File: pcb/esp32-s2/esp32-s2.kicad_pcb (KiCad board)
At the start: 2 copper layers, 31 parts, among them J1 BATT, J2 HALL-CONN, Q1 BC817, Q2 BC807, SW1 WIFI-Config, SW2 RST, U1 XC6220, U2 ESP32-S2-WROOM

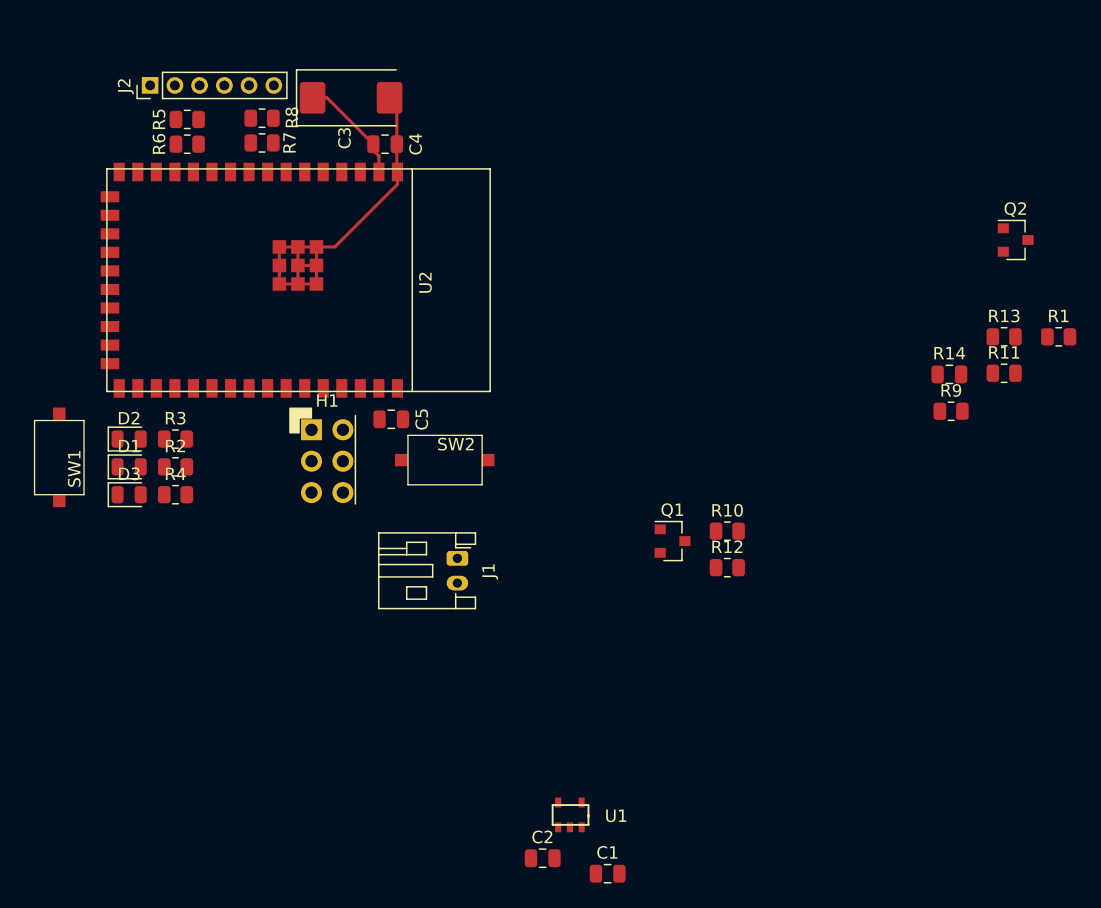
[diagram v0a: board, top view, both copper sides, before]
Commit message: update pcb for esp32s2
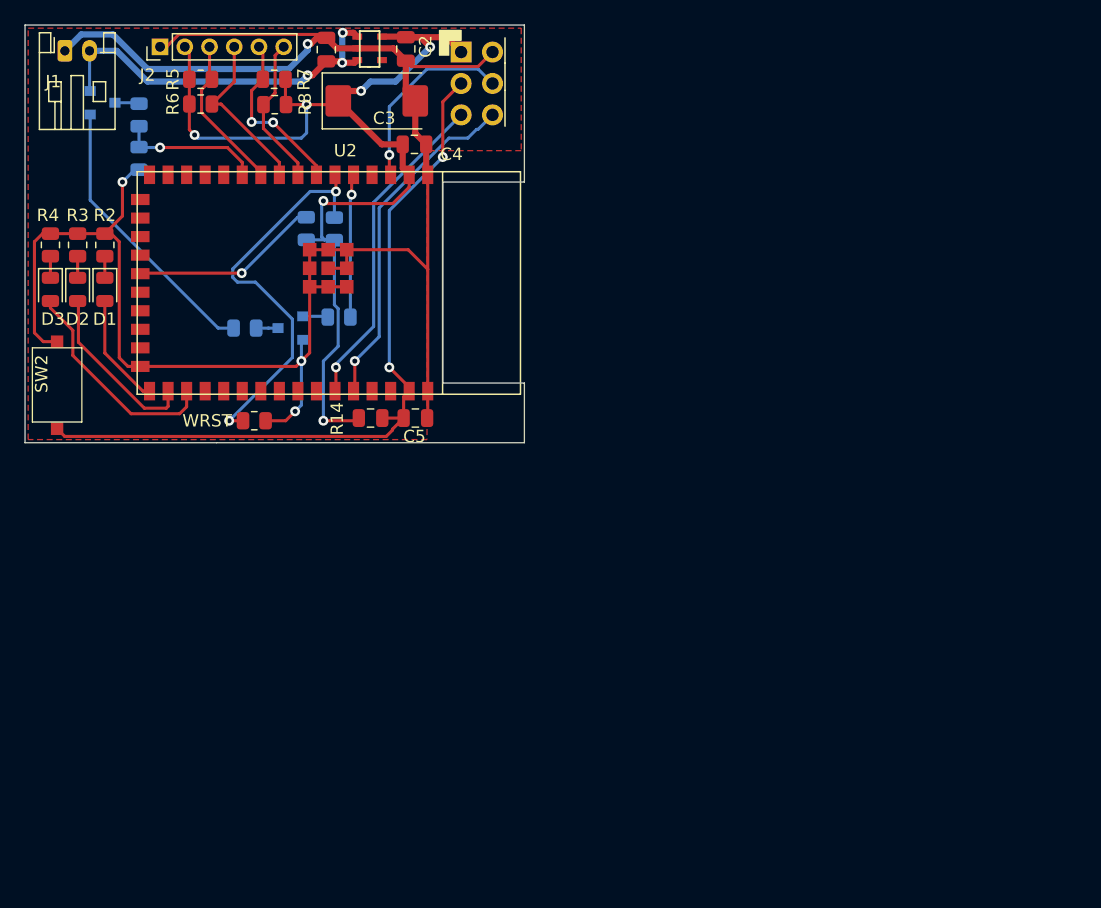
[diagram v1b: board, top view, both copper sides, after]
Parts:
- removed SW1: WIFI-Config, SMDButton:SMD_Button
- added R15: 0, Resistor_SMD:R_0805_2012Metric, F.Cu at (106.2, 86.9)
- Q1, Q2, R1, R10, R11, R12, R13, R9: moved to B.Cu
- moved Q2 74.7 mm to (93.9, 61.1)
- moved R13 71.4 mm to (96.8, 65.7), turned to 270 degrees
- moved C1 70.4 mm to (112.0, 56.9), turned to 90 degrees
- moved C2 66.4 mm to (118.4, 56.8), turned to 270 degrees
- moved U1 64.0 mm to (115.5, 56.8), turned to 270 degrees
- moved R11 61.5 mm to (105.4, 79.4)
- moved R1 61.5 mm to (110.4, 71.3), turned to 90 degrees
- moved R12 60.0 mm to (96.8, 62.1), turned to 270 degrees
- moved R9 52.0 mm to (112.7, 71.3), turned to 270 degrees
- moved J1 51.9 mm to (90.8, 57.0), turned to 0 degrees
- moved R14 46.9 mm to (115.6, 86.7)
- moved R10 35.9 mm to (113.0, 78.5)
- moved Q1 35.4 mm to (109.1, 79.4), turned to 180 degrees
- moved H1 32.9 mm to (122.9, 57.0)
- moved SW2 32.0 mm to (90.4, 83.8), turned to 90 degrees
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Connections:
- U2 pad 10: HALL4 -> HALL3
- U2 pad 8: HALL2 -> HALL4
- U2 pad 9: HALL3 -> HALL2
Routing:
- net GND: track 32.4 -> 165.5 mm, vias 0 -> 4
- net VCC: track 8.90 -> 85.6 mm, vias 0 -> 6
- net /EN: track 0.00 -> 61.0 mm, vias 0 -> 2
- net Net-(R15-Pad2): track 0.00 -> 32.9 mm, vias 0 -> 2
- net BATT: track 0.00 -> 30.5 mm, vias 0 -> 3
- net /RX: track 0.00 -> 28.0 mm, vias 0 -> 1
- net /TX: track 0.00 -> 26.6 mm, vias 0 -> 1
- net Net-(Q2-Pad1): track 0.00 -> 22.8 mm
- net /Green: track 0.00 -> 17.8 mm
- net IO0: track 0.00 -> 15.6 mm, vias 0 -> 1
- net Net-(R1-Pad2): track 0.00 -> 15.3 mm, vias 0 -> 1
- net /Red: track 0.00 -> 14.1 mm
- net HALL1: track 0.00 -> 14.0 mm, vias 0 -> 2
- net HALL2: track 0.00 -> 13.8 mm
- net HALL3: track 0.00 -> 12.8 mm
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- added copper zone on F.Cu, net GND
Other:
- board outline added: 40.4 x 33.8 mm
- board text added: "WRST"
